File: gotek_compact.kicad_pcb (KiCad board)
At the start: 2 copper layers, 54.6 x 41.9 mm, 32 parts, among them IC1 STM32F105RBT6, IC2 74AHCT08D, IC3 AP7381-33Y-13, X1 8MHz

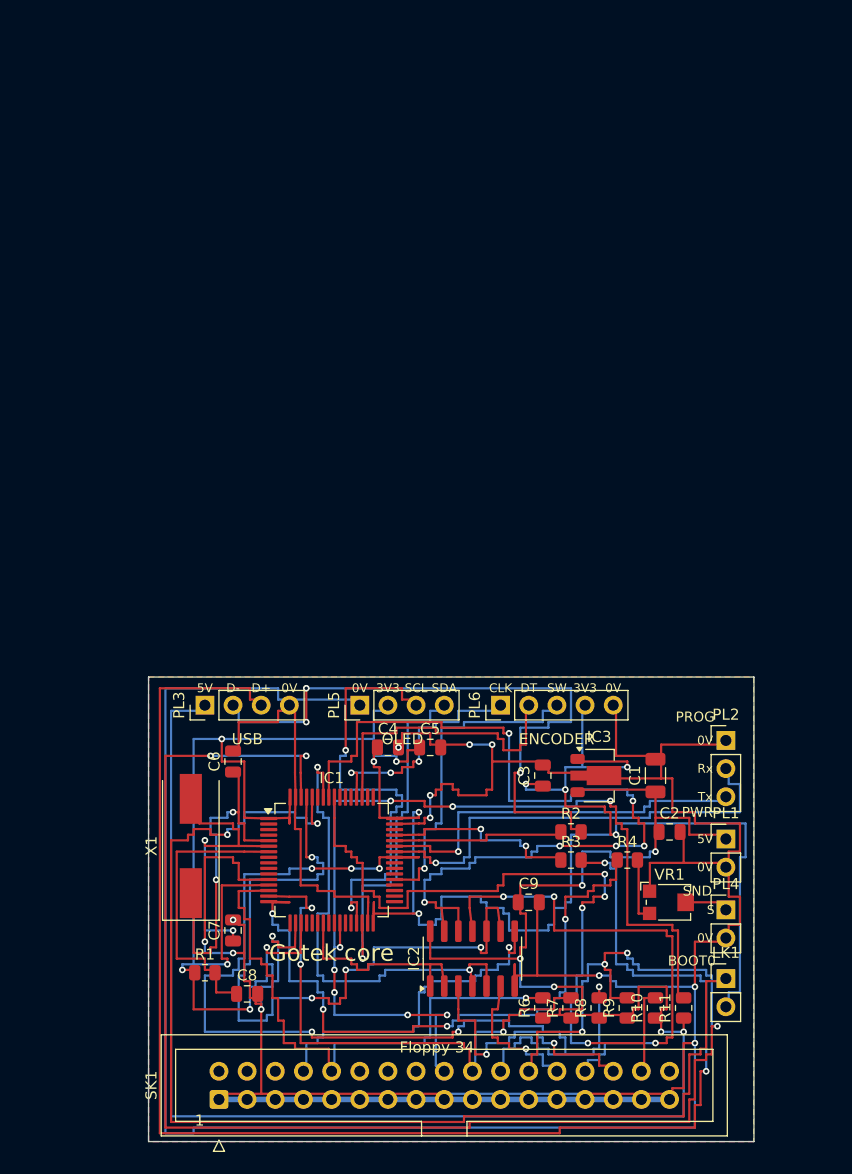
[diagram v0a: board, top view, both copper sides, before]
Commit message: Updated Schematics and initial PCB placement
Schematics have been re-done based on OpenFlop from SukkoPera, with changes towards more compact design.
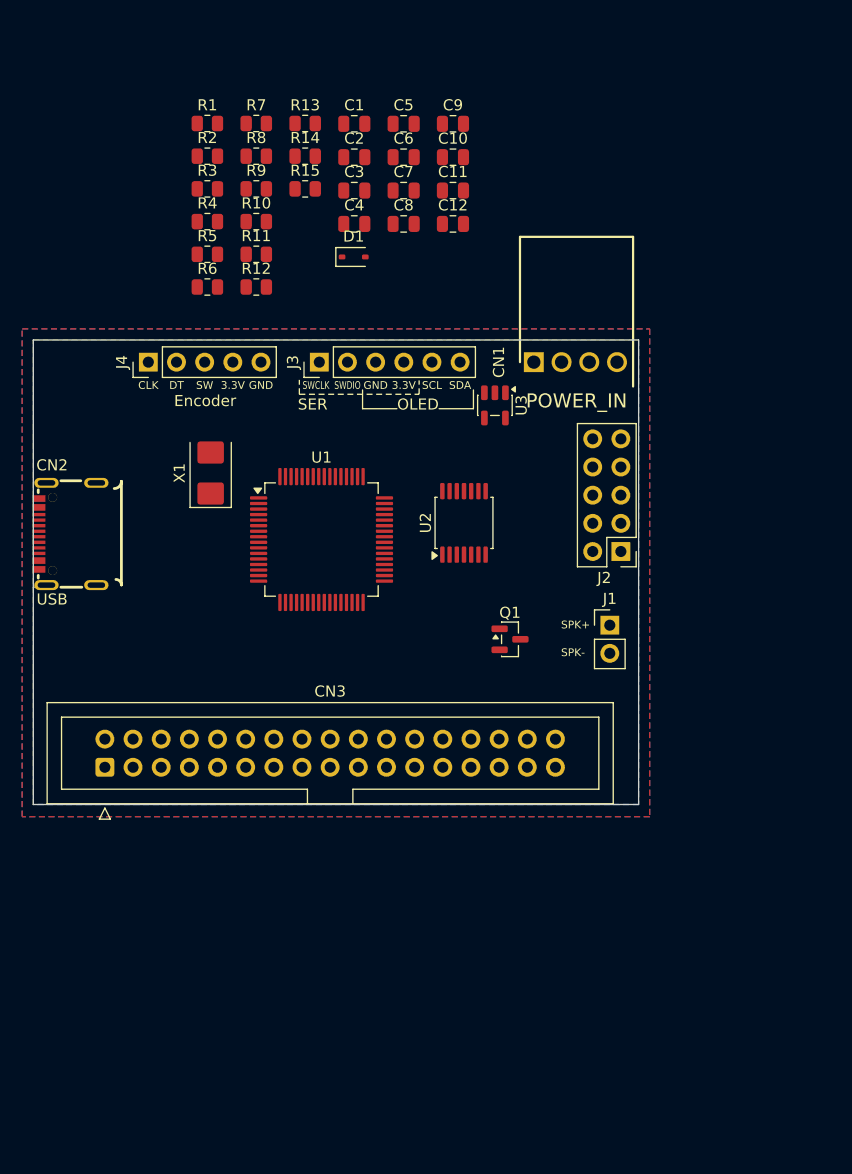
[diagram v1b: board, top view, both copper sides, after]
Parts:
- removed IC1: STM32F105RBT6, LQFP-64_10x10mm_P0.5mm
- removed IC2: 74AHCT08D, SOIC-14_3.9x8.7mm_P1.27mm
- removed IC3: AP7381-33Y-13, SOT-89-3
- removed LK1: BOOT0, PinHeader_1x02_P2.54mm_Vertical
- removed PL1: Power 5V, PinHeader_1x02_P2.54mm_Vertical
- removed PL2: Program, PinHeader_1x03_P2.54mm_Vertical
- removed PL3: USB, PinHeader_1x04_P2.54mm_Vertical
- removed PL4: Sound, PinHeader_1x02_P2.54mm_Vertical
- removed PL5: OLED, PinHeader_1x04_P2.54mm_Vertical
- removed PL6: Encoder, PinHeader_1x05_P2.54mm_Vertical
- removed SK1: Floppy 34, IDC-Header_2x17_P2.54mm_Vertical
- removed VR1: 10K, Potentiometer_Bourns_TC33X_Vertical
- added C10: 100nF, Capacitor_SMD:C_0805_2012Metric, F.Cu at (77.5, 3.12)
- added C11: 22pF, Capacitor_SMD:C_0805_2012Metric, F.Cu at (77.5, 6.12)
- added C12: 22pF, Capacitor_SMD:C_0805_2012Metric, F.Cu at (77.5, 9.13)
- added CN1: POWER_IN, gotek_compact:171826-4, F.Cu at (84.8, 21.6)
- added CN2: USB, gotek_compact:USB-C-SMD_GT-USB-7016, F.Cu at (42.7, 37.1)
- added CN3: Floppy 34, Connector_IDC:IDC-Header_2x17_P2.54mm_Vertical, F.Cu at (46.1, 58.1)
- added D1: 1N4148WS, Diode_SMD:D_SOD-323, F.Cu at (68.5, 12.1)
- added J1: Sound, Connector_PinHeader_2.54mm:PinHeader_1x02_P2.54mm_Vertical, F.Cu at (91.6, 45.3)
- added J2: USB_Prog, Connector_PinHeader_2.54mm:PinHeader_2x05_P2.54mm_Vertical, F.Cu at (92.6, 38.7)
- added J3: OLED+SER, Connector_PinHeader_2.54mm:PinHeader_1x06_P2.54mm_Vertical, F.Cu at (65.4, 21.6)
- added J4: Encoder, Connector_PinHeader_2.54mm:PinHeader_1x05_P2.54mm_Vertical, F.Cu at (50.0, 21.6)
- added Q1: MMBT3904, Package_TO_SOT_SMD:SOT-23, F.Cu at (82.6, 46.6)
- added R12: 22, Resistor_SMD:R_0805_2012Metric, F.Cu at (59.7, 14.8)
- added R13: 1K, Resistor_SMD:R_0805_2012Metric, F.Cu at (64.1, 0.07)
- added R14: 5K1, Resistor_SMD:R_0805_2012Metric, F.Cu at (64.1, 3.02)
- added R15: 5K1, Resistor_SMD:R_0805_2012Metric, F.Cu at (64.1, 5.97)
- added R5: 4K7, Resistor_SMD:R_0805_2012Metric, F.Cu at (55.3, 11.9)
- added U1: STM32F105RBT6, Package_QFP:LQFP-64_10x10mm_P0.5mm, F.Cu at (65.6, 37.6)
- added U2: 74LCX07, Package_SO:TSSOP-14_4.4x5mm_P0.65mm, F.Cu at (78.5, 36.1)
- added U3: AP2112K-3.3, Package_TO_SOT_SMD:SOT-23-5, F.Cu at (81.2, 25.5)
- C1: value 10uF/16V -> 1uF; footprint C_1206_3216Metric -> Capacitor_SMD:C_0805_2012Metric
- C2: value 100nF -> 10uF; footprint C_0805_2012Metric -> Capacitor_SMD:C_0805_2012Metric
- C3: value 2u2 -> 10uF; footprint C_0805_2012Metric -> Capacitor_SMD:C_0805_2012Metric
- C4, C5, C8, C9: footprint C_0805_2012Metric -> Capacitor_SMD:C_0805_2012Metric
- C6, C7: value 22pF -> 100nF; footprint C_0805_2012Metric -> Capacitor_SMD:C_0805_2012Metric
- R1, R2, R3, R4: footprint R_0805_2012Metric -> Resistor_SMD:R_0805_2012Metric
- R10, R11, R6, R7, R8, R9: value 1K0 -> 1K; footprint R_0805_2012Metric -> Resistor_SMD:R_0805_2012Metric
- X1: footprint Crystal_SMD_HC49-SD -> Crystal:Crystal_SMD_5032-2Pin_5.0x3.2mm
- moved R7 84.7 mm to (59.7, 0.07), turned to 0 degrees
- moved R8 82.8 mm to (59.7, 3.02), turned to 0 degrees
- moved R9 81.1 mm to (59.7, 5.97), turned to 0 degrees
- moved R10 79.5 mm to (59.7, 8.93), turned to 0 degrees
- moved R11 78.1 mm to (59.7, 11.9), turned to 0 degrees
- moved R1 76.6 mm to (55.3, 0.07)
- moved R6 71.7 mm to (55.3, 14.8), turned to 0 degrees
- moved C8 70.9 mm to (73.0, 9.13)
- moved C9 70.5 mm to (77.5, 0.10)
- moved R2 69.2 mm to (55.3, 3.02)
- moved R4 68.9 mm to (55.3, 8.93)
- moved R3 68.8 mm to (55.3, 5.97)
- moved C7 68.5 mm to (73.0, 6.12), turned to 0 degrees
- moved C2 67.2 mm to (68.6, 3.12)
- moved C1 64.8 mm to (68.6, 0.10), turned to 0 degrees
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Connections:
- C2 pad 1: +5V -> +3V3
- C4 pad 1: +3V3 -> GND
- C4 pad 2: GND -> +3V3
- C5 pad 1: +3V3 -> GND
- C5 pad 2: GND -> +3V3
- C6 pad 1: OSC_IN -> GND
- C6 pad 2: GND -> +3V3
- C7 pad 1: OSC_OUT -> GND
- C7 pad 2: GND -> +3V3
- C8 pad 1: NRST -> GND
- C8 pad 2: GND -> +3V3
- C9 pad 1: +5V -> GND
- C9 pad 2: GND -> +3V3
- R1 pad 1: +3V3 -> NRST
- R1 pad 2: NRST -> +3V3
- R10 pad 1: +5V -> _SIDE
- R10 pad 2: SIDE_SELECT -> +5V
- R11 pad 1: +5V -> DIR
- R11 pad 2: DIRECTION -> +5V
- R2 pad 1: USB_DM_MCU -> Net-(U1-PA11)
- R2 pad 2: USB_DM -> USB_D-
- R3 pad 1: USB_DP_MCU -> Net-(U1-PA12)
- R3 pad 2: USB_DP -> USB_D+
- R4 pad 1: SOUNDER -> GND
- R4 pad 2: SOUND_POT -> BOOT0
- R6 pad 1: +5V -> _SEL0
- R6 pad 2: DRIVE_SELECT_0 -> +5V
- R7 pad 1: +5V -> _STEP
- R7 pad 2: STEP -> +5V
- R8 pad 1: +5V -> _DKWD
- R8 pad 2: WRITE_DATA -> +5V
- R9 pad 1: +5V -> _DKWE
- R9 pad 2: WRITE_ENABLE -> +5V
- X1 pad 1: OSC_IN -> /OSC_IN
- X1 pad 2: OSC_OUT -> /OSC_OUT
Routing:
- net GND: track 407.2 -> 0.00 mm, vias 13 -> 0
- net +3V3: track 228.3 -> 0.00 mm, vias 13 -> 0
- net +5V: track 174.7 -> 0.00 mm, vias 6 -> 0
- net WRITE_ENABLE: track 147.5 -> 0.00 mm, vias 6 -> 0
- net USB_DP: track 134.6 -> 0.00 mm, vias 2 -> 0
- net BOOT0: track 108.5 -> 0.00 mm, vias 2 -> 0
- net WRITE_DATA: track 94.7 -> 0.00 mm, vias 6 -> 0
- net DIRECTION: track 88.1 -> 0.00 mm, vias 8 -> 0
- net WP_3V: track 81.1 -> 0.00 mm, vias 6 -> 0
- net SIDE_SELECT: track 68.9 -> 0.00 mm, vias 4 -> 0
- net INDEX_3V: track 67.0 -> 0.00 mm, vias 4 -> 0
- net SOUNDER: track 61.3 -> 0.00 mm, vias 4 -> 0
- net USB_DM: track 57.9 -> 0.00 mm, vias 3 -> 0
- net DRIVE_SELECT_0: track 51.0 -> 0.00 mm, vias 1 -> 0
- net STEP: track 49.6 -> 0.00 mm, vias 3 -> 0
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- added copper zone on In1.Cu, net GND
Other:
- copper layers 2 -> 4
- board text added: "3.3V"
- board text added: "GND"
- board text added: "SER"
- board text added: "SPK+"
- board text added: "SPK-"
- board text added: "SWCLK"
- board text added: "SWDIO"
- board text removed: "0V"
- board text removed: "1"
- board text removed: "3V3"
- board text removed: "5V"
- board text removed: "BOOT0"
- board text removed: "D+"
- board text removed: "D-"
- board text removed: "ENCODER"
- board text removed: "Floppy 34"
- board text removed: "Gotek core"
- board text removed: "PROG"
- board text removed: "PWR"
- board text removed: "Rx"
- board text removed: "S"
- board text removed: "SND"
- board text removed: "Tx"
- board text removed: "USB"

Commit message: USB connector changed
USB connector changed to a model without elevation
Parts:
- CN2: footprint gotek_compact:USB-C-SMD_GT-USB-7016 -> gotek_compact:USB-C-SMD_TYPE-C16PIN
- moved Q1 3.96 mm to (78.9, 45.1)
- moved CN1 3.27 mm to (85.4, 24.8)
- moved CN2 2.83 mm to (45.1, 35.6), turned to -90 degrees
- moved U3 2.81 mm to (79.0, 27.1)
- moved J2 2.52 mm to (92.9, 41.2)
- moved C10 1.55 mm to (77.9, 1.61)
- moved C6 1.55 mm to (73.4, 1.61)
- moved C11 1.55 mm to (77.9, 4.62)
- moved C12 1.55 mm to (77.9, 7.63)
- moved C5 1.55 mm to (73.4, -1.40)
- moved C7 1.55 mm to (73.4, 4.62)
- moved C8 1.55 mm to (73.4, 7.63)
- moved C9 1.55 mm to (77.9, -1.40)
- moved D1 1.55 mm to (68.9, 10.6)
- moved J4 1.55 mm to (50.4, 20.1)
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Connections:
- R14 pad 2: GND -> +5V
- R15 pad 2: GND -> +5V
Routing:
- added copper zone on In2.Cu, net +3V3
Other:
- board size 54.6 x 41.9 mm -> 54.6 x 42 mm

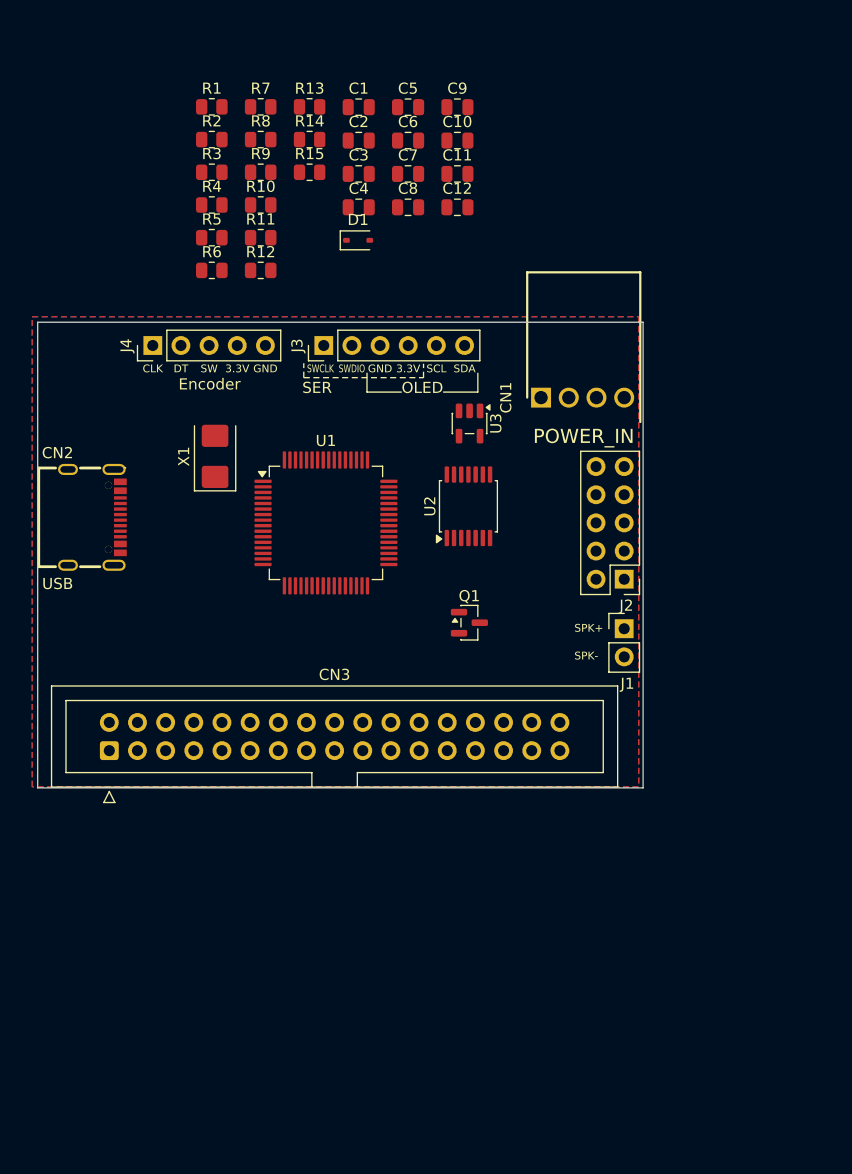
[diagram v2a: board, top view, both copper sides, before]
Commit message: A few component value changes
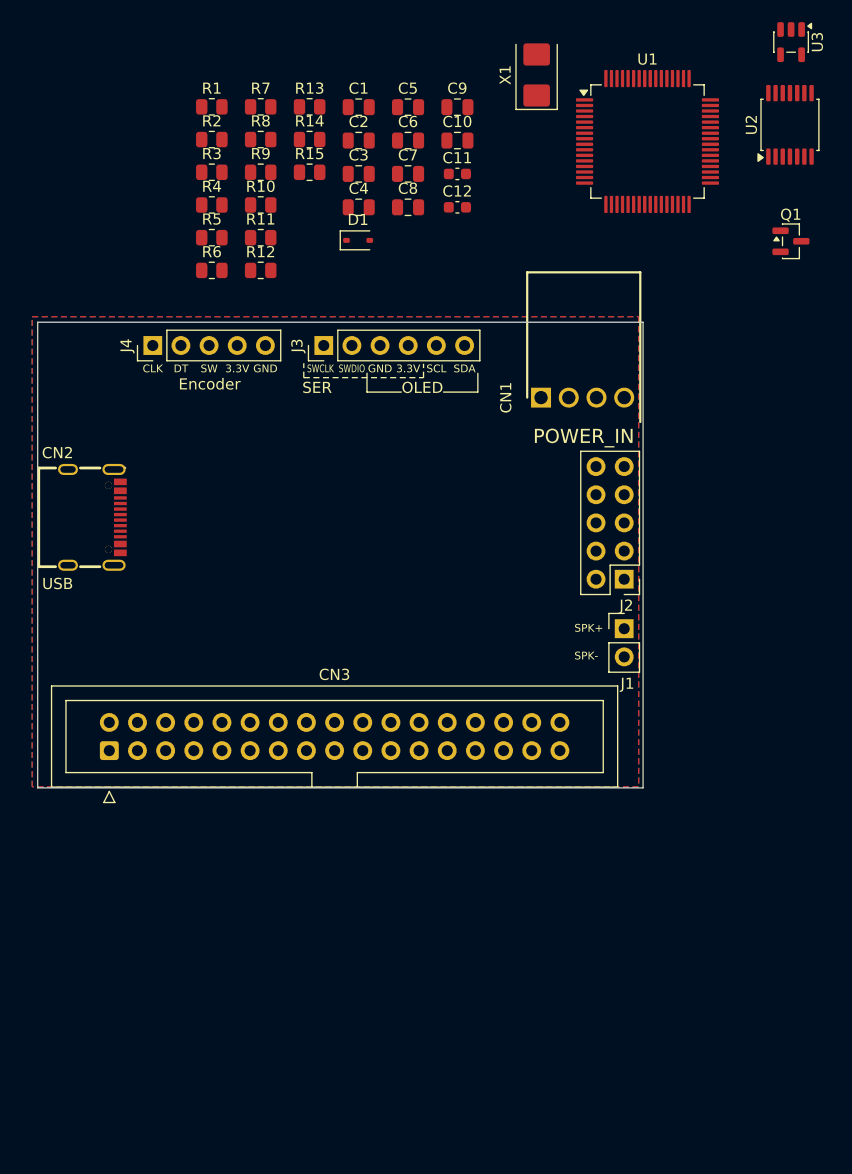
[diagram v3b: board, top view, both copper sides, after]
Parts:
- C11, C12: value 22pF -> 30pF; footprint Capacitor_SMD:C_0805_2012Metric -> Capacitor_SMD:C_0603_1608Metric
- R14, R15: value 5K1 -> 51K
- moved Q1 45.0 mm to (107.9, 10.7)
- moved U1 45.0 mm to (95.0, 1.70)
- moved U2 45.0 mm to (107.8, 0.20)
- moved U3 45.0 mm to (108.0, -7.26)
- moved X1 45.0 mm to (85.0, -4.30)

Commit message: PCB routing finished
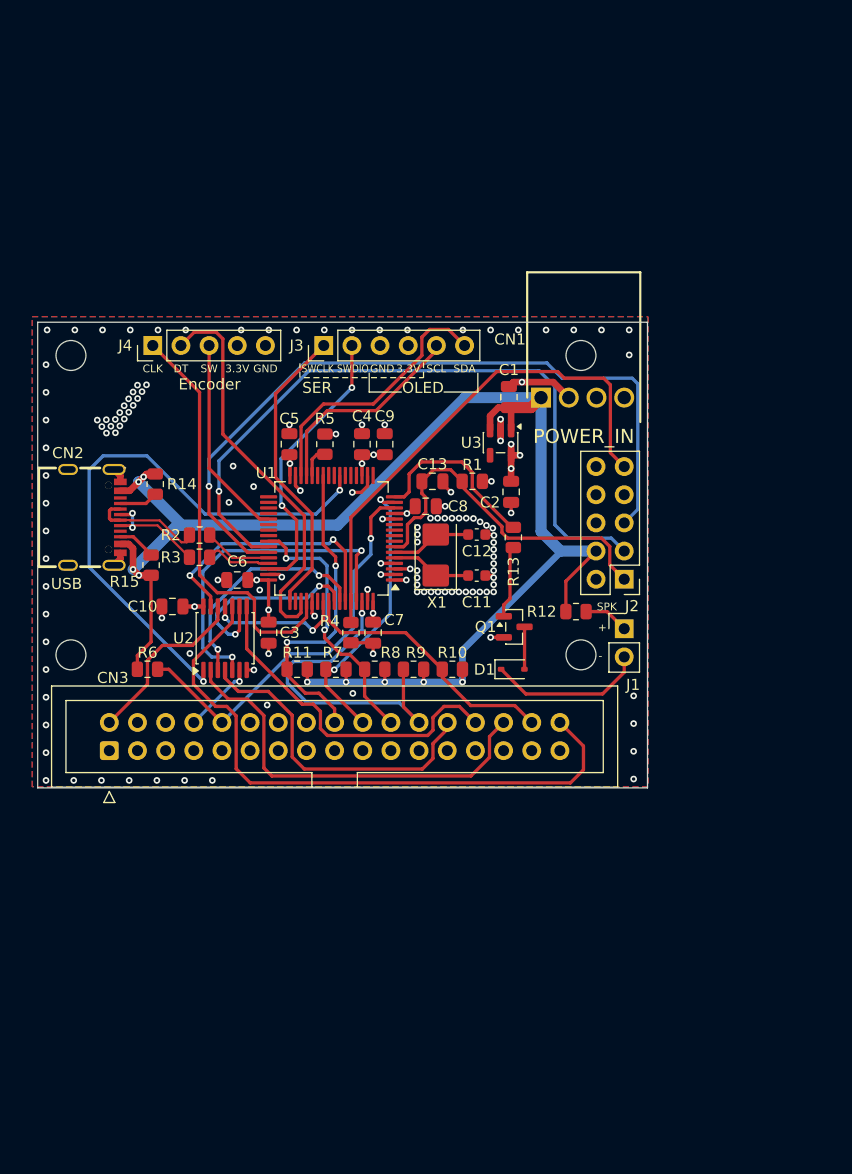
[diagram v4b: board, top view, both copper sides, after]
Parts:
- added C9: 10uF, Capacitor_SMD:C_0805_2012Metric, F.Cu at (71.3, 29.0)
- added H1: Mounting Hole, MountingHole:MountingHole_2.7mm_M2.5, F.Cu at (43.0, 21.0)
- added H2: Mounting Hole, MountingHole:MountingHole_2.7mm_M2.5, F.Cu at (43.0, 48.0)
- added H3: Mounting Hole, MountingHole:MountingHole_2.7mm_M2.5, F.Cu at (89.0, 48.0)
- added H4: Mounting Hole, MountingHole:MountingHole_2.7mm_M2.5, F.Cu at (89.0, 21.0)
- moved U2 68.8 mm to (56.9, 46.5)
- moved C10 51.9 mm to (52.1, 43.6)
- moved R7 51.2 mm to (66.9, 49.3)
- moved R8 48.9 mm to (70.4, 49.3)
- moved R9 46.9 mm to (73.9, 49.3)
- moved U1 45.8 mm to (66.5, 37.5), turned to 180 degrees
- moved R10 45.3 mm to (77.4, 49.3)
- moved U3 44.6 mm to (81.8, 28.9)
- moved X1 44.2 mm to (75.9, 39.0)
- moved R13 43.0 mm to (82.9, 37.4), turned to -90 degrees
- moved Q1 42.8 mm to (83.0, 45.5)
- moved C6 42.5 mm to (58.0, 41.2)
- moved C3 42.2 mm to (60.8, 46.0), turned to -90 degrees
- moved R12 41.9 mm to (88.5, 44.1), turned to 180 degrees
- moved C7 41.5 mm to (70.2, 46.0), turned to 90 degrees
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- renumbered C9 to C10, C10 to C13
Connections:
- net Net-(U1-PA11) renamed USB_ST_D-
- net Net-(U1-PA12) renamed USB_ST_D+
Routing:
- net +5V: track 0.00 -> 138.1 mm, vias 0 -> 9
- net TXD: track 0.00 -> 67.9 mm, vias 0 -> 1
- net RXD: track 0.00 -> 64.5 mm, vias 0 -> 1
- net _RDY: track 0.00 -> 55.8 mm
- net _DKRD_3V: track 0.00 -> 51.9 mm, vias 0 -> 2
- net BOOT0: track 0.00 -> 46.7 mm
- net GND: track 0.00 -> 39.3 mm, vias 0 -> 134
- net ENC_CLK: track 0.00 -> 37.6 mm
- net _DKRD: track 0.00 -> 36.9 mm
- net _SEL0: track 0.00 -> 36.3 mm, vias 0 -> 1
- net ENC_DT: track 0.00 -> 36.2 mm
- net NRST: track 0.00 -> 32.4 mm
- net _WPROT: track 0.00 -> 31.0 mm
- net _INDEX_3V: track 0.00 -> 30.9 mm, vias 0 -> 2
- net _DKWE: track 0.00 -> 30.9 mm, vias 0 -> 1
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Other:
- board size 54.6 x 42 mm -> 55 x 42 mm
- board text added: "+"
- board text added: "-"
- board text added: "SPK"
- board text removed: "SPK+"
- board text removed: "SPK-"
